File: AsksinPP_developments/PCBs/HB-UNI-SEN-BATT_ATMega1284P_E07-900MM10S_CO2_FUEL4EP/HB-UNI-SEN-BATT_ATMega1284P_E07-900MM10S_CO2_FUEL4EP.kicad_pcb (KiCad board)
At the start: 2 copper layers, 75 x 75 mm, 81 parts, among them J1 Conn_01x02, J10 charge, J11 ePaper connector, J12 FTDI Debuger, J13 U.FL connector, J2 Conn_01x02, J3 Conn_01x02, J4 Conn_01x02, J5 ISP Programmer, Q1 IRLU024N, Q2 FDN304P, Q3 FDN304P, Q4 FDN304P, SW1 Config button, SW2 Reset button, U1 ATmega1284P-AU, U2 TPS61221DCK, U3 BME280, Y1 8MHz

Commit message: PCB updates
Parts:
- D1: value LED red 3mm -> LED red SMD
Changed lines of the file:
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@@
 			)
 		)
-		(property "Value" "LED red 3mm"
+		(property "Value" "LED red SMD"
 			(at -1.9595 1.397 0)
 			(layer "F.Fab")
@@
 		(sheetname "Stammblatt")
 		(sheetfile "HB-UNI-SEN-BATT_ATMega1284P_E07-900MM10S_CO2_FUEL4EP.kicad_sch")
-		(attr through_hole exclude_from_pos_files)
+		(attr through_hole)
 		(fp_line
 			(start -1.12 -1.39)
@@
 		(sheetname "Stammblatt")
 		(sheetfile "HB-UNI-SEN-BATT_ATMega1284P_E07-900MM10S_CO2_FUEL4EP.kicad_sch")
-		(attr exclude_from_bom)
+		(attr exclude_from_pos_files exclude_from_bom)
 		(fp_circle
 			(center 0 0)
@@
 		(sheetname "Stammblatt")
 		(sheetfile "HB-UNI-SEN-BATT_ATMega1284P_E07-900MM10S_CO2_FUEL4EP.kicad_sch")
-		(attr exclude_from_bom)
+		(attr exclude_from_pos_files exclude_from_bom)
 		(fp_circle
 			(center 0 0)
@@
 		(sheetname "Stammblatt")
 		(sheetfile "HB-UNI-SEN-BATT_ATMega1284P_E07-900MM10S_CO2_FUEL4EP.kicad_sch")
-		(attr exclude_from_bom)
+		(attr exclude_from_pos_files exclude_from_bom)
 		(fp_circle
 			(center 0 0)
@@
 		(sheetname "Stammblatt")
 		(sheetfile "HB-UNI-SEN-BATT_ATMega1284P_E07-900MM10S_CO2_FUEL4EP.kicad_sch")
-		(attr exclude_from_bom)
+		(attr exclude_from_pos_files exclude_from_bom)
 		(fp_circle
 			(center 0 0)
@@
 		(sheetname "Stammblatt")
 		(sheetfile "HB-UNI-SEN-BATT_ATMega1284P_E07-900MM10S_CO2_FUEL4EP.kicad_sch")
-		(attr through_hole exclude_from_bom)
+		(attr through_hole exclude_from_pos_files exclude_from_bom)
 		(fp_line
 			(start 54.62 -8.565)
@@
 		(sheetname "Stammblatt")
 		(sheetfile "HB-UNI-SEN-BATT_ATMega1284P_E07-900MM10S_CO2_FUEL4EP.kicad_sch")
-		(attr through_hole exclude_from_bom)
+		(attr through_hole exclude_from_pos_files exclude_from_bom)
 		(fp_line
 			(start -2.62 8.565)
@@
 		(sheetname "Stammblatt")
 		(sheetfile "HB-UNI-SEN-BATT_ATMega1284P_E07-900MM10S_CO2_FUEL4EP.kicad_sch")
-		(attr through_hole exclude_from_bom)
+		(attr through_hole exclude_from_pos_files exclude_from_bom)
 		(fp_poly
 			(pts
@@
 		(sheetname "Stammblatt")
 		(sheetfile "HB-UNI-SEN-BATT_ATMega1284P_E07-900MM10S_CO2_FUEL4EP.kicad_sch")
-		(attr through_hole)
+		(attr through_hole exclude_from_pos_files)
 		(fp_line
 			(start -1.06 15.06)
@@
 		(sheetname "Stammblatt")
 		(sheetfile "HB-UNI-SEN-BATT_ATMega1284P_E07-900MM10S_CO2_FUEL4EP.kicad_sch")
-		(attr through_hole exclude_from_bom)
+		(attr through_hole exclude_from_pos_files exclude_from_bom)
 		(fp_circle
 			(center 0 0)
@@
 		(sheetname "Stammblatt")
 		(sheetfile "HB-UNI-SEN-BATT_ATMega1284P_E07-900MM10S_CO2_FUEL4EP.kicad_sch")
-		(attr through_hole exclude_from_bom)
+		(attr through_hole exclude_from_pos_files exclude_from_bom)
 		(fp_circle
 			(center 0 0)
@@
 		(sheetname "Stammblatt")
 		(sheetfile "HB-UNI-SEN-BATT_ATMega1284P_E07-900MM10S_CO2_FUEL4EP.kicad_sch")
-		(attr through_hole exclude_from_bom)
+		(attr through_hole exclude_from_pos_files exclude_from_bom)
 		(fp_circle
 			(center 0 0)
@@
 		(sheetname "Stammblatt")
 		(sheetfile "HB-UNI-SEN-BATT_ATMega1284P_E07-900MM10S_CO2_FUEL4EP.kicad_sch")
-		(attr through_hole exclude_from_bom)
+		(attr through_hole exclude_from_pos_files exclude_from_bom)
 		(fp_circle
 			(center 0 0)
@@
 			)
 		)
-		(property "TYPE" "LED_0805"
+		(property "TYPE" ""
 			(at 0 0 0)
 			(unlocked yes)
@@
 			)
 		)
-		(property "LCSC" "C84256"
+		(property "LCSC" ""
 			(at 0 0 0)
 			(unlocked yes)
@@
 		(sheetname "Stammblatt")
 		(sheetfile "HB-UNI-SEN-BATT_ATMega1284P_E07-900MM10S_CO2_FUEL4EP.kicad_sch")
-		(attr through_hole)
+		(attr through_hole exclude_from_pos_files)
 		(fp_line
 			(start -0.29 -1.236)
@@
 			)
 		)
-		(property "TYPE" "LED_0805"
+		(property "TYPE" ""
 			(at 0 0 0)
 			(unlocked yes)
@@
 			)
 		)
-		(property "LCSC" "C84256"
+		(property "LCSC" ""
 			(at 0 0 0)
 			(unlocked yes)
@@
 		(sheetname "Stammblatt")
 		(sheetfile "HB-UNI-SEN-BATT_ATMega1284P_E07-900MM10S_CO2_FUEL4EP.kicad_sch")
-		(attr through_hole)
+		(attr through_hole exclude_from_pos_files)
 		(fp_line
 			(start -0.29 -1.236)
@@
 			)
 		)
-		(property "TYPE" "LED_0805"
+		(property "TYPE" ""
 			(at 0 0 0)
 			(unlocked yes)
@@
 			)
 		)
-		(property "LCSC" "C84256"
+		(property "LCSC" ""
 			(at 0 0 0)
 			(unlocked yes)
@@
 		(sheetname "Stammblatt")
 		(sheetfile "HB-UNI-SEN-BATT_ATMega1284P_E07-900MM10S_CO2_FUEL4EP.kicad_sch")
-		(attr through_hole)
+		(attr through_hole exclude_from_pos_files)
 		(fp_line
 			(start -0.29 -1.236)
@@
 		(sheetname "Stammblatt")
 		(sheetfile "HB-UNI-SEN-BATT_ATMega1284P_E07-900MM10S_CO2_FUEL4EP.kicad_sch")
-		(attr through_hole)
+		(attr through_hole exclude_from_pos_files)
 		(fp_line
 			(start 0 0)
@@
 		(sheetname "Stammblatt")
 		(sheetfile "HB-UNI-SEN-BATT_ATMega1284P_E07-900MM10S_CO2_FUEL4EP.kicad_sch")
-		(attr smd)
+		(attr smd exclude_from_pos_files)
 		(fp_line
 			(start 6.9 -6.7)
@@
 		(width 1)
 		(layer "F.Cu")
-		(net 18)
-	)
-	(segment
-		(start 65.78 -65.9)
-		(end 65.95 -65.9)
-		(width 1)
-		(layer "F.Cu")

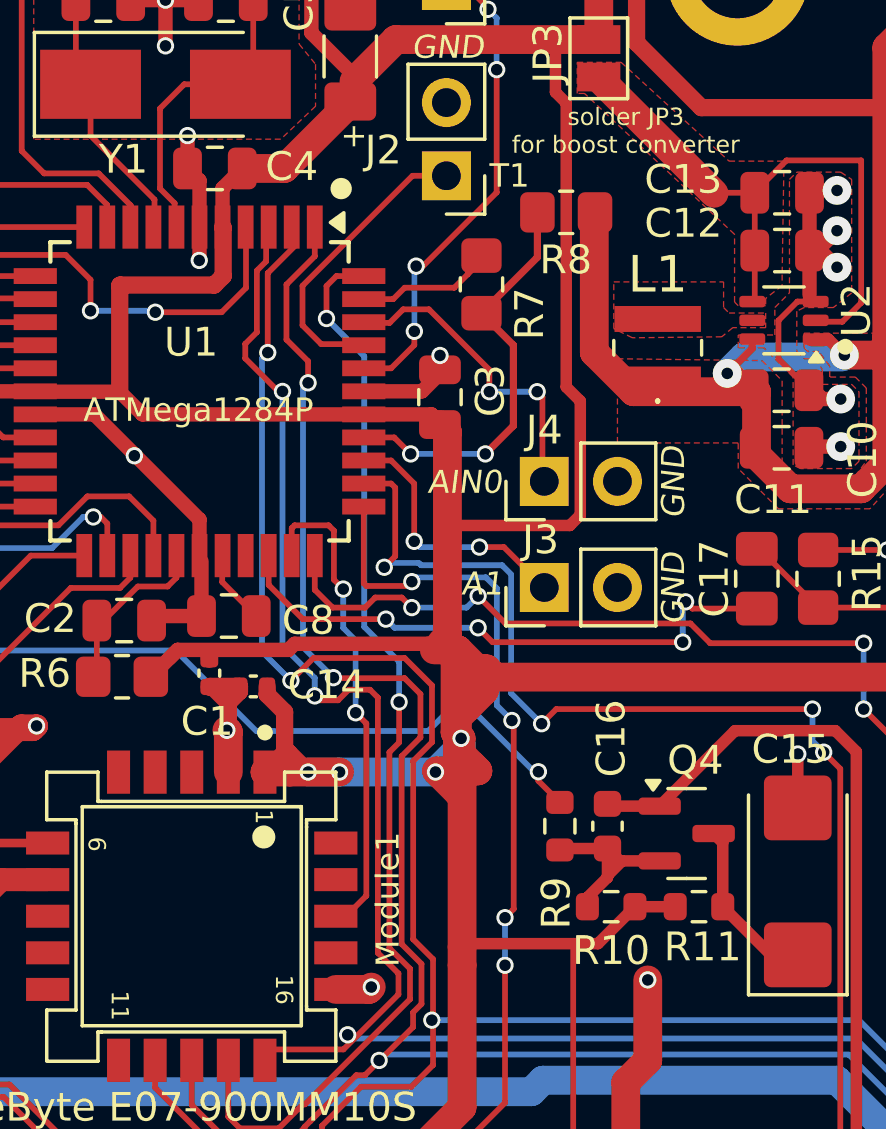
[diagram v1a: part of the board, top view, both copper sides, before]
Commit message: HB-UNI-SEN-BATT_ATMega1284P_E07-900MM10S_CO2_FUEL4EP: added warning in README.md not to uuse because of fatal  errors of PCB
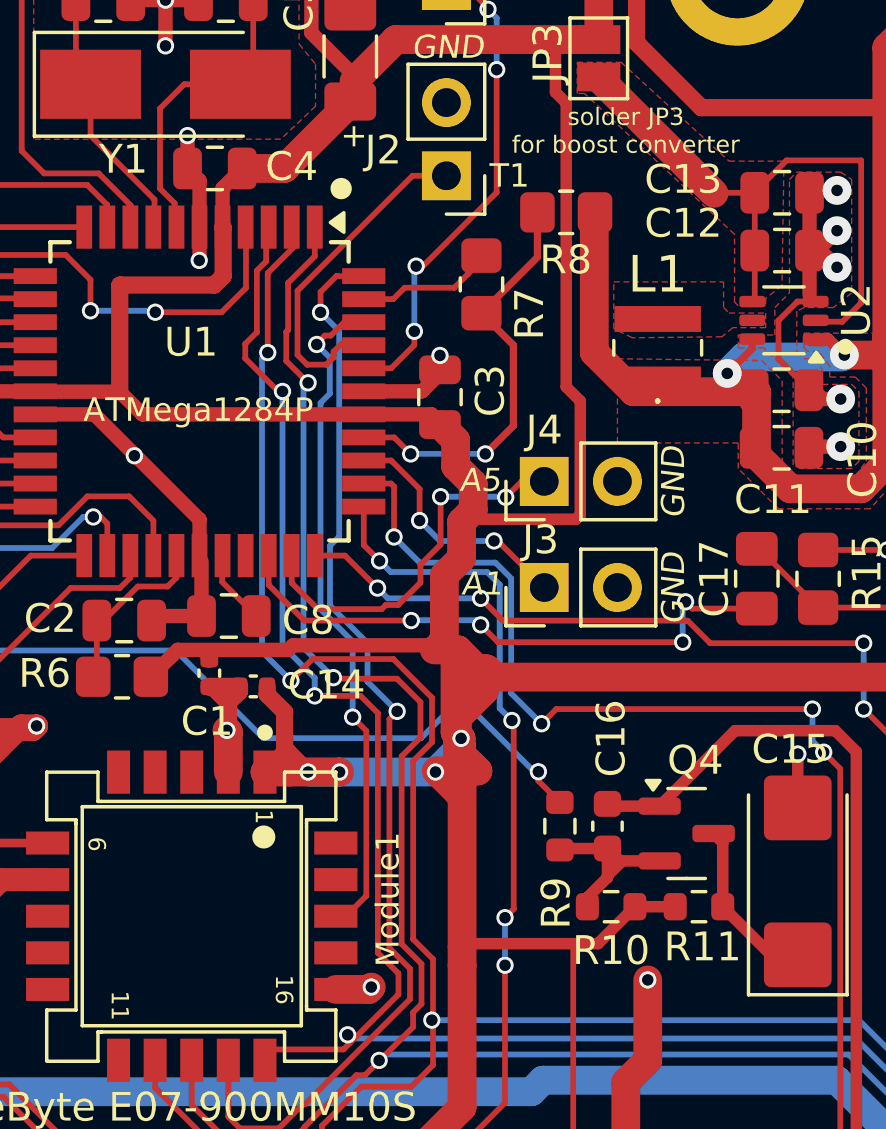
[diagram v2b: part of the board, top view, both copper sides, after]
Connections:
- J4 pad 1: /AIN0 -> /A5
- Module1 pad 3D: /A5 -> /INT2
- U1 pad 42: /AIN0 -> /INT2
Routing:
- net /INT2: track 0.00 -> 23.1 mm, vias 0 -> 2
- net /AIN0: track 10.9 -> 0.00 mm, vias 2 -> 0
- net /A5: track 16.7 -> 13.3 mm
- net /PB1_T1: track 9.59 -> 11.1 mm
- net /A2: track 52.7 -> 51.4 mm
- net /A4: track 61.8 -> 60.5 mm
- net /A3: track 32.8 -> 31.9 mm
- net /SCK: track 80.4 -> 79.8 mm
- net /A1: track 9.08 -> 8.55 mm
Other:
- board text added: "A5"
- board text added: "Version 1.1 - 05/2026 (KiCAD 8)"
- board text removed: "AIN0"
- board text removed: "Version 1.0 - 06/2025 (KiCAD 8)"
